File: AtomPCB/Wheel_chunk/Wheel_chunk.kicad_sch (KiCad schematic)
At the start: 16 parts, among them J1 DF40HC_4.0_-40DS-0.4V_70_, J2 Conn_01x04_Pin, J3 Conn_01x04_Pin, J4 Conn_01x04_Pin, J5 Conn_01x04_Pin, U1 ATtiny416-M, U3 DRV8834RGER, U4 DRV8834RGER, U6 MPM3610AGQV-P

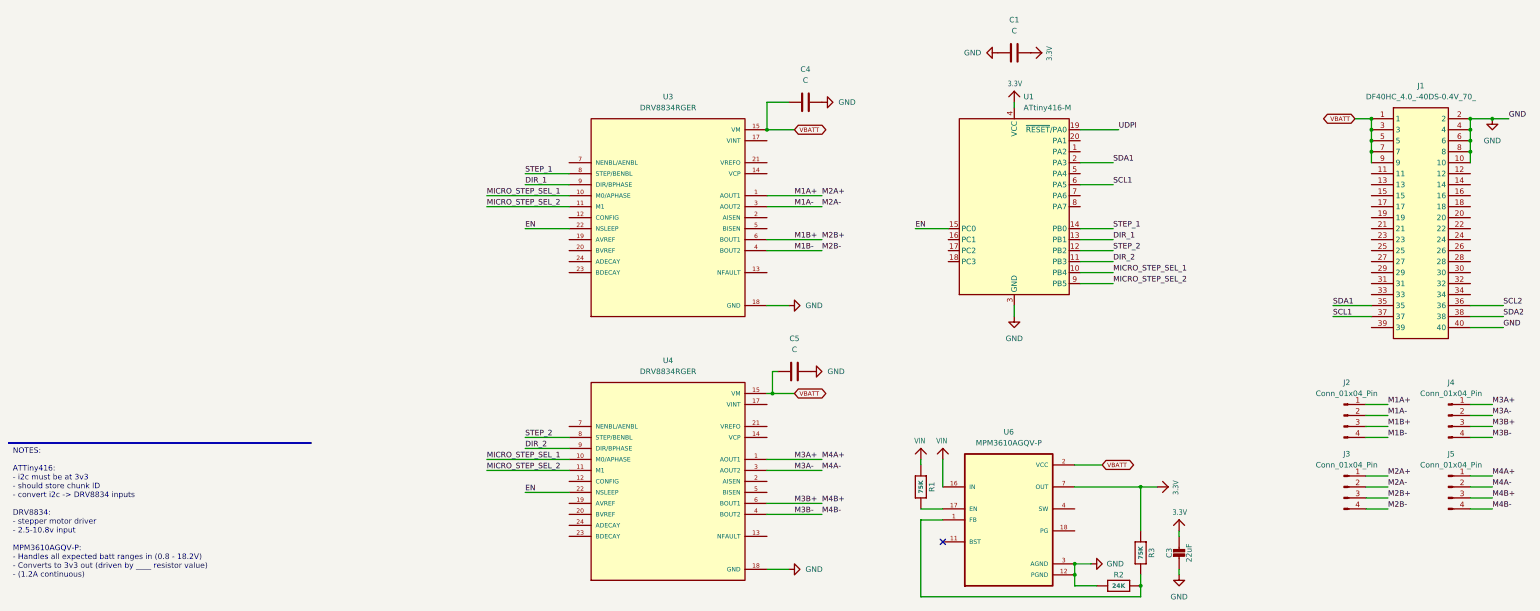
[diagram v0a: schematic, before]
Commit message: adding core pcb templates. Finished rev 0.1 of wheel chunk pcb
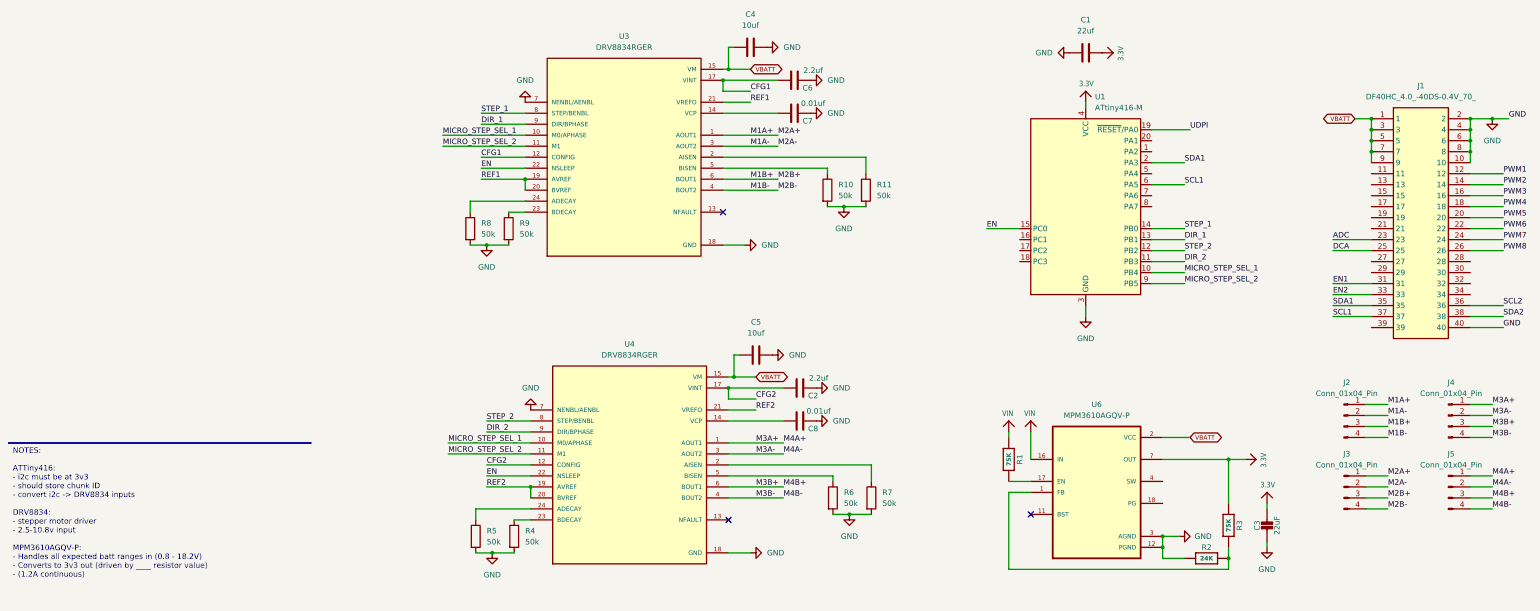
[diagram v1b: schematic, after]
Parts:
- added C2, C6: 2.2uf, Capacitor_SMD:C_0805_2012Metric, symbol Device:C
- added C7, C8: 0.01uf, Capacitor_SMD:C_0805_2012Metric, symbol Device:C
- added R10, R11, R4, R5, R6, R7, R8, R9: 50k, Resistor_SMD:R_0805_2012Metric, symbol Device:R
- C1: value C -> 22uf; footprint (none) -> Capacitor_SMD:C_0805_2012Metric
- C3: footprint Wheel_chunk:0805-NO -> Capacitor_SMD:C_0805_2012Metric
- C4, C5: value C -> 10uf; footprint (none) -> Capacitor_SMD:C_0805_2012Metric
- J1: footprint DF40HC4040DS04V70 -> HIROSE_DF40HC_40_connector:DF40HC4040DS04V70
- J2, J3, J4, J5: footprint Connector_PinHeader_1.00mm:PinHeader_1x04_P1.00mm_Vertical -> Wire_flat_pads:PAD_1x4_4.0x2.0
- R1, R2, R3: footprint Wheel_chunk:0603-NO -> Resistor_SMD:R_0805_2012Metric
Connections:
- net GND: now also U3.7 (NENBL/AENBL), U4.7 (NENBL/AENBL), C2.2, C6.2, C7.2, C8.2, R10.2, R11.2, R4.2, R5.2, R6.2, R7.2, R8.2, R9.2
- net CFG2: now reaches U4.12 (CONFIG)
- net CFG2: now also U4.17 (VINT), C2.1
- net at U4.14 (VCP): now also C8.1
- net REF2: now reaches U4.19 (AVREF)
- net REF2: now also U4.20 (BVREF), U4.21 (VREFO)
- net at U4.2 (AISEN): now also R7.1
- net at U4.23 (BDECAY): now also R4.1
- net at U4.24 (ADECAY): now also R5.1
- net at U4.5 (BISEN): now also R6.1
- net CFG1: now reaches U3.12 (CONFIG)
- net CFG1: now also U3.17 (VINT), C6.1
- net at U3.14 (VCP): now also C7.1
- net REF1: now reaches U3.19 (AVREF)
- net REF1: now also U3.20 (BVREF), U3.21 (VREFO)
- net at U3.2 (AISEN): now also R11.1
- net at U3.23 (BDECAY): now also R9.1
- net at U3.24 (ADECAY): now also R8.1
- net at U3.5 (BISEN): now also R10.1
- net PWM1: now reaches J1.12
- net PWM2: now reaches J1.14
- net PWM3: now reaches J1.16
- net PWM4: now reaches J1.18
- net PWM5: now reaches J1.20
- net PWM6: now reaches J1.22
- net ADC: now reaches J1.23
- net PWM7: now reaches J1.24
- net DCA: now reaches J1.25
- net PWM8: now reaches J1.26
- net EN1: now reaches J1.31
- net EN2: now reaches J1.33
- no-connect marks 1 -> 3
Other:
- moved on the sheet: C1, C3, C5, R1, R2, R3, U1, U4, U6
